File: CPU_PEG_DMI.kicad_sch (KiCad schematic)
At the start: 2 parts

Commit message: stroopwafel.exe
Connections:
- net DMI_CRx_PTx_0+: no longer JCPU1.Y3 (DMI_RXP_0)
- net DMI_CRx_PTx_0-: no longer JCPU1.Y4 (DMI_RXN_0)
- net DMI_CRx_PTx_1+: no longer JCPU1.AA4 (DMI_RXP_1)
- net DMI_CRx_PTx_1-: no longer JCPU1.AA5 (DMI_RXN_1)
- net DMI_CRx_PTx_2+: no longer JCPU1.AB4 (DMI_RXP_2)
- net DMI_CRx_PTx_2-: no longer JCPU1.AB3 (DMI_RXN_2)
- net DMI_CRx_PTx_3+: no longer JCPU1.AC4 (DMI_RXP_3)
- net DMI_CRx_PTx_3-: no longer JCPU1.AC5 (DMI_RXN_3)
- net DMI_CTx_PRx_0+: no longer JCPU1.AC2 (DMI_TXP_0)
- net DMI_CTx_PRx_0-: no longer JCPU1.AC1 (DMI_TXN_0)
- net DMI_CTx_PRx_1+: no longer JCPU1.AD3 (DMI_TXP_1)
- net DMI_CTx_PRx_1-: no longer JCPU1.AD2 (DMI_TXN_1)
- net DMI_CTx_PRx_2+: no longer JCPU1.AE2 (DMI_TXP_2)
- net DMI_CTx_PRx_2-: no longer JCPU1.AE1 (DMI_TXN_2)
- net DMI_CTx_PRx_3+: no longer JCPU1.AF2 (DMI_TXP_3)
- net DMI_CTx_PRx_3-: no longer JCPU1.AF3 (DMI_TXN_3)
- net PCIe_CPU_Rx0+: no longer JCPU1.B8 (PEG_RXP_0)
- net PCIe_CPU_Rx0-: no longer JCPU1.B7 (PEG_RXN_0)
- net PCIe_CPU_Rx1+: no longer JCPU1.C7 (PEG_RXP_1)
- net PCIe_CPU_Rx1-: no longer JCPU1.C6 (PEG_RXN_1)
- net PCIe_CPU_Rx10+: no longer JCPU1.M6 (PEG_RXP_10)
- net PCIe_CPU_Rx10-: no longer JCPU1.M5 (PEG_RXN_10)
- net PCIe_CPU_Rx11+: no longer JCPU1.N5 (PEG_RXP_11)
- net PCIe_CPU_Rx11-: no longer JCPU1.N4 (PEG_RXN_11)
- net PCIe_CPU_Rx12+: no longer JCPU1.P6 (PEG_RXP_12)
- net PCIe_CPU_Rx12-: no longer JCPU1.P5 (PEG_RXN_12)
- net PCIe_CPU_Rx13+: no longer JCPU1.R5 (PEG_RXP_13)
- net PCIe_CPU_Rx13-: no longer JCPU1.R4 (PEG_RXN_13)
- net PCIe_CPU_Rx14+: no longer JCPU1.T6 (PEG_RXP_14)
- net PCIe_CPU_Rx14-: no longer JCPU1.T5 (PEG_RXN_14)
- net PCIe_CPU_Rx15+: no longer JCPU1.U5 (PEG_RXP_15)
- net PCIe_CPU_Rx15-: no longer JCPU1.U4 (PEG_RXN_15)
- net PCIe_CPU_Rx2+: no longer JCPU1.D6 (PEG_RXP_2)
- net PCIe_CPU_Rx2-: no longer JCPU1.D5 (PEG_RXN_2)
- net PCIe_CPU_Rx3+: no longer JCPU1.E5 (PEG_RXP_3)
- net PCIe_CPU_Rx3-: no longer JCPU1.E4 (PEG_RXN_3)
- net PCIe_CPU_Rx4+: no longer JCPU1.F6 (PEG_RXP_4)
- net PCIe_CPU_Rx4-: no longer JCPU1.F5 (PEG_RXN_4)
- net PCIe_CPU_Rx5+: no longer JCPU1.G5 (PEG_RXP_5)
- net PCIe_CPU_Rx5-: no longer JCPU1.G4 (PEG_RXN_5)
- net PCIe_CPU_Rx6+: no longer JCPU1.H6 (PEG_RXP_6)
- net PCIe_CPU_Rx6-: no longer JCPU1.H5 (PEG_RXN_6)
- net PCIe_CPU_Rx7+: no longer JCPU1.J5 (PEG_RXP_7)
- net PCIe_CPU_Rx7-: no longer JCPU1.J4 (PEG_RXN_7)
- net PCIe_CPU_Rx8+: no longer JCPU1.K6 (PEG_RXP_8)
- net PCIe_CPU_Rx8-: no longer JCPU1.K5 (PEG_RXN_8)
- net PCIe_CPU_Rx9+: no longer JCPU1.L5 (PEG_RXP_9)
- net PCIe_CPU_Rx9-: no longer JCPU1.L4 (PEG_RXN_9)
- net PCIe_CPU_Tx0+: no longer JCPU1.A5 (PEG_TXP_0)
- net PCIe_CPU_Tx0-: no longer JCPU1.A6 (PEG_TXN_0)
- net PCIe_CPU_Tx1+: no longer JCPU1.B4 (PEG_TXP_1)
- net PCIe_CPU_Tx1-: no longer JCPU1.B5 (PEG_TXN_1)
- net PCIe_CPU_Tx10+: no longer JCPU1.L1 (PEG_TXP_10)
- net PCIe_CPU_Tx10-: no longer JCPU1.L2 (PEG_TXN_10)
- net PCIe_CPU_Tx11+: no longer JCPU1.M2 (PEG_TXP_11)
- net PCIe_CPU_Tx11-: no longer JCPU1.M3 (PEG_TXN_11)
- net PCIe_CPU_Tx12+: no longer JCPU1.N1 (PEG_TXP_12)
- net PCIe_CPU_Tx12-: no longer JCPU1.N2 (PEG_TXN_12)
- net PCIe_CPU_Tx13+: no longer JCPU1.P2 (PEG_TXP_13)
- net PCIe_CPU_Tx13-: no longer JCPU1.P3 (PEG_TXN_13)
- net PCIe_CPU_Tx14+: no longer JCPU1.R2 (PEG_TXP_14)
- net PCIe_CPU_Tx14-: no longer JCPU1.R1 (PEG_TXN_14)
- net PCIe_CPU_Tx15+: no longer JCPU1.T2 (PEG_TXP_15)
- net PCIe_CPU_Tx15-: no longer JCPU1.T3 (PEG_TXN_15)
- net PCIe_CPU_Tx2+: no longer JCPU1.C3 (PEG_TXP_2)
- net PCIe_CPU_Tx2-: no longer JCPU1.C4 (PEG_TXN_2)
- net PCIe_CPU_Tx3+: no longer JCPU1.D2 (PEG_TXP_3)
- net PCIe_CPU_Tx3-: no longer JCPU1.D3 (PEG_TXN_3)
- net PCIe_CPU_Tx4+: no longer JCPU1.E1 (PEG_TXP_4)
- net PCIe_CPU_Tx4-: no longer JCPU1.E2 (PEG_TXN_4)
- net PCIe_CPU_Tx5+: no longer JCPU1.F2 (PEG_TXP_5)
- net PCIe_CPU_Tx5-: no longer JCPU1.F3 (PEG_TXN_5)
- net PCIe_CPU_Tx6+: no longer JCPU1.G1 (PEG_TXP_6)
- net PCIe_CPU_Tx6-: no longer JCPU1.G2 (PEG_TXN_6)
- net PCIe_CPU_Tx7+: no longer JCPU1.H2 (PEG_TXP_7)
- net PCIe_CPU_Tx7-: no longer JCPU1.H3 (PEG_TXN_7)
- net PCIe_CPU_Tx8+: no longer JCPU1.J1 (PEG_TXP_8)
- net PCIe_CPU_Tx8-: no longer JCPU1.J2 (PEG_TXN_8)
- net PCIe_CPU_Tx9+: no longer JCPU1.K2 (PEG_TXP_9)
- net PCIe_CPU_Tx9-: no longer JCPU1.K3 (PEG_TXN_9)
- net at R10.2: no longer JCPU1.L7 (PEG_RCOMP)
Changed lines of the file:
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@@
 		(lib_id "A-my-stuff:Intel_CFL_1151")
 		(at 116.84 114.3 0)
-		(unit 3)
+		(unit 1)
 		(exclude_from_sim no)
 		(in_bom yes)
@@
 		(pin "J5"
 		)
-		(instances
-			(project ""
-				(path "/4bc771b8-eb19-46d0-8798-27231a7c6e83/061fe2d6-87c2-48c2-90bb-0928700512fc"
-					(reference "JCPU1")
-					(unit 3)
-				)
-			)
-		)
 	)

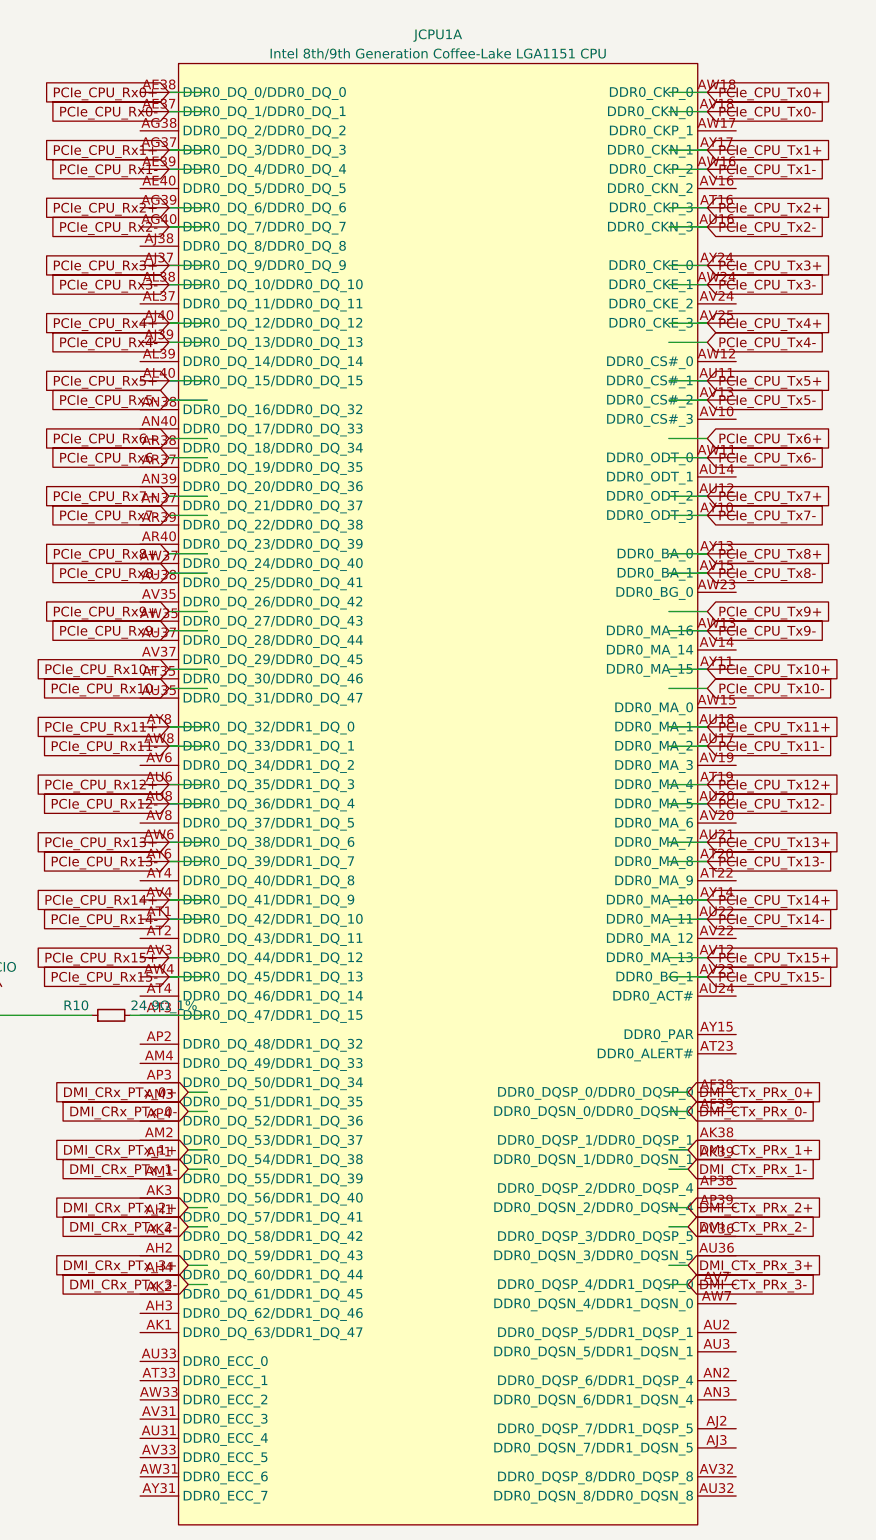
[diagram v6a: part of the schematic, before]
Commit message: Fixed entire schematic being broken
somehow every symbol with index 1 broke and updating the pcb stopped working. how does that even happen. oh well it's fixed now
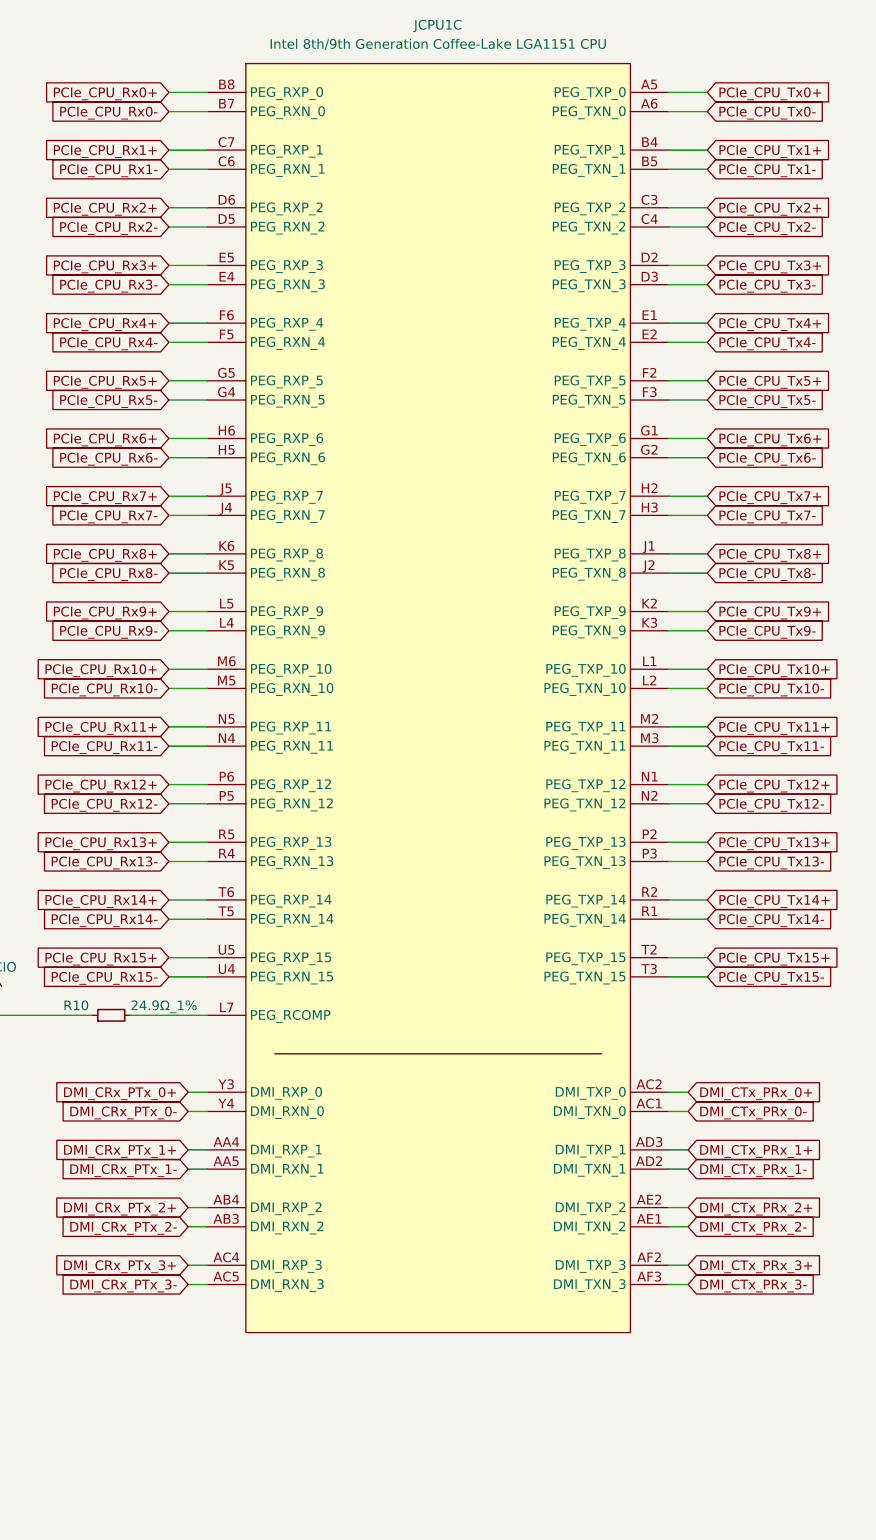
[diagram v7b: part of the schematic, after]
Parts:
- removed JCPU1: Intel 8th/9th Generation Coffee-Lake LGA1151 CPU, A-my-stuff:LGA-1151_L47.1-W42.5-P0.91_PE115127-4041-01H, symbol A-my-stuff:Intel_CFL_1151
- added JCPU1: Intel 8th/9th Generation Coffee-Lake LGA1151 CPU, A-my-stuff:LGA-1151_L47.1-W42.5-P0.91_PE115127-4041-01H, symbol A-my-stuff:Intel_CFL_1151
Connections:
- net DMI_CRx_PTx_0+: now also JCPU1.Y3 (DMI_RXP_0)
- net DMI_CRx_PTx_0-: now also JCPU1.Y4 (DMI_RXN_0)
- net DMI_CRx_PTx_1+: now also JCPU1.AA4 (DMI_RXP_1)
- net DMI_CRx_PTx_1-: now also JCPU1.AA5 (DMI_RXN_1)
- net DMI_CRx_PTx_2+: now also JCPU1.AB4 (DMI_RXP_2)
- net DMI_CRx_PTx_2-: now also JCPU1.AB3 (DMI_RXN_2)
- net DMI_CRx_PTx_3+: now also JCPU1.AC4 (DMI_RXP_3)
- net DMI_CRx_PTx_3-: now also JCPU1.AC5 (DMI_RXN_3)
- net DMI_CTx_PRx_0+: now also JCPU1.AC2 (DMI_TXP_0)
- net DMI_CTx_PRx_0-: now also JCPU1.AC1 (DMI_TXN_0)
- net DMI_CTx_PRx_1+: now also JCPU1.AD3 (DMI_TXP_1)
- net DMI_CTx_PRx_1-: now also JCPU1.AD2 (DMI_TXN_1)
- net DMI_CTx_PRx_2+: now also JCPU1.AE2 (DMI_TXP_2)
- net DMI_CTx_PRx_2-: now also JCPU1.AE1 (DMI_TXN_2)
- net DMI_CTx_PRx_3+: now also JCPU1.AF2 (DMI_TXP_3)
- net DMI_CTx_PRx_3-: now also JCPU1.AF3 (DMI_TXN_3)
- net PCIe_CPU_Rx0+: now also JCPU1.B8 (PEG_RXP_0)
- net PCIe_CPU_Rx0-: now also JCPU1.B7 (PEG_RXN_0)
- net PCIe_CPU_Rx1+: now also JCPU1.C7 (PEG_RXP_1)
- net PCIe_CPU_Rx1-: now also JCPU1.C6 (PEG_RXN_1)
- net PCIe_CPU_Rx10+: now also JCPU1.M6 (PEG_RXP_10)
- net PCIe_CPU_Rx10-: now also JCPU1.M5 (PEG_RXN_10)
- net PCIe_CPU_Rx11+: now also JCPU1.N5 (PEG_RXP_11)
- net PCIe_CPU_Rx11-: now also JCPU1.N4 (PEG_RXN_11)
- net PCIe_CPU_Rx12+: now also JCPU1.P6 (PEG_RXP_12)
- net PCIe_CPU_Rx12-: now also JCPU1.P5 (PEG_RXN_12)
- net PCIe_CPU_Rx13+: now also JCPU1.R5 (PEG_RXP_13)
- net PCIe_CPU_Rx13-: now also JCPU1.R4 (PEG_RXN_13)
- net PCIe_CPU_Rx14+: now also JCPU1.T6 (PEG_RXP_14)
- net PCIe_CPU_Rx14-: now also JCPU1.T5 (PEG_RXN_14)
- net PCIe_CPU_Rx15+: now also JCPU1.U5 (PEG_RXP_15)
- net PCIe_CPU_Rx15-: now also JCPU1.U4 (PEG_RXN_15)
- net PCIe_CPU_Rx2+: now also JCPU1.D6 (PEG_RXP_2)
- net PCIe_CPU_Rx2-: now also JCPU1.D5 (PEG_RXN_2)
- net PCIe_CPU_Rx3+: now also JCPU1.E5 (PEG_RXP_3)
- net PCIe_CPU_Rx3-: now also JCPU1.E4 (PEG_RXN_3)
- net PCIe_CPU_Rx4+: now also JCPU1.F6 (PEG_RXP_4)
- net PCIe_CPU_Rx4-: now also JCPU1.F5 (PEG_RXN_4)
- net PCIe_CPU_Rx5+: now also JCPU1.G5 (PEG_RXP_5)
- net PCIe_CPU_Rx5-: now also JCPU1.G4 (PEG_RXN_5)
- net PCIe_CPU_Rx6+: now also JCPU1.H6 (PEG_RXP_6)
- net PCIe_CPU_Rx6-: now also JCPU1.H5 (PEG_RXN_6)
- net PCIe_CPU_Rx7+: now also JCPU1.J5 (PEG_RXP_7)
- net PCIe_CPU_Rx7-: now also JCPU1.J4 (PEG_RXN_7)
- net PCIe_CPU_Rx8+: now also JCPU1.K6 (PEG_RXP_8)
- net PCIe_CPU_Rx8-: now also JCPU1.K5 (PEG_RXN_8)
- net PCIe_CPU_Rx9+: now also JCPU1.L5 (PEG_RXP_9)
- net PCIe_CPU_Rx9-: now also JCPU1.L4 (PEG_RXN_9)
- net PCIe_CPU_Tx0+: now also JCPU1.A5 (PEG_TXP_0)
- net PCIe_CPU_Tx0-: now also JCPU1.A6 (PEG_TXN_0)
- net PCIe_CPU_Tx1+: now also JCPU1.B4 (PEG_TXP_1)
- net PCIe_CPU_Tx1-: now also JCPU1.B5 (PEG_TXN_1)
- net PCIe_CPU_Tx10+: now also JCPU1.L1 (PEG_TXP_10)
- net PCIe_CPU_Tx10-: now also JCPU1.L2 (PEG_TXN_10)
- net PCIe_CPU_Tx11+: now also JCPU1.M2 (PEG_TXP_11)
- net PCIe_CPU_Tx11-: now also JCPU1.M3 (PEG_TXN_11)
- net PCIe_CPU_Tx12+: now also JCPU1.N1 (PEG_TXP_12)
- net PCIe_CPU_Tx12-: now also JCPU1.N2 (PEG_TXN_12)
- net PCIe_CPU_Tx13+: now also JCPU1.P2 (PEG_TXP_13)
- net PCIe_CPU_Tx13-: now also JCPU1.P3 (PEG_TXN_13)
- net PCIe_CPU_Tx14+: now also JCPU1.R2 (PEG_TXP_14)
- net PCIe_CPU_Tx14-: now also JCPU1.R1 (PEG_TXN_14)
- net PCIe_CPU_Tx15+: now also JCPU1.T2 (PEG_TXP_15)
- net PCIe_CPU_Tx15-: now also JCPU1.T3 (PEG_TXN_15)
- net PCIe_CPU_Tx2+: now also JCPU1.C3 (PEG_TXP_2)
- net PCIe_CPU_Tx2-: now also JCPU1.C4 (PEG_TXN_2)
- net PCIe_CPU_Tx3+: now also JCPU1.D2 (PEG_TXP_3)
- net PCIe_CPU_Tx3-: now also JCPU1.D3 (PEG_TXN_3)
- net PCIe_CPU_Tx4+: now also JCPU1.E1 (PEG_TXP_4)
- net PCIe_CPU_Tx4-: now also JCPU1.E2 (PEG_TXN_4)
- net PCIe_CPU_Tx5+: now also JCPU1.F2 (PEG_TXP_5)
- net PCIe_CPU_Tx5-: now also JCPU1.F3 (PEG_TXN_5)
- net PCIe_CPU_Tx6+: now also JCPU1.G1 (PEG_TXP_6)
- net PCIe_CPU_Tx6-: now also JCPU1.G2 (PEG_TXN_6)
- net PCIe_CPU_Tx7+: now also JCPU1.H2 (PEG_TXP_7)
- net PCIe_CPU_Tx7-: now also JCPU1.H3 (PEG_TXN_7)
- net PCIe_CPU_Tx8+: now also JCPU1.J1 (PEG_TXP_8)
- net PCIe_CPU_Tx8-: now also JCPU1.J2 (PEG_TXN_8)
- net PCIe_CPU_Tx9+: now also JCPU1.K2 (PEG_TXP_9)
- net PCIe_CPU_Tx9-: now also JCPU1.K3 (PEG_TXN_9)
- net at R10.2: now also JCPU1.L7 (PEG_RCOMP)

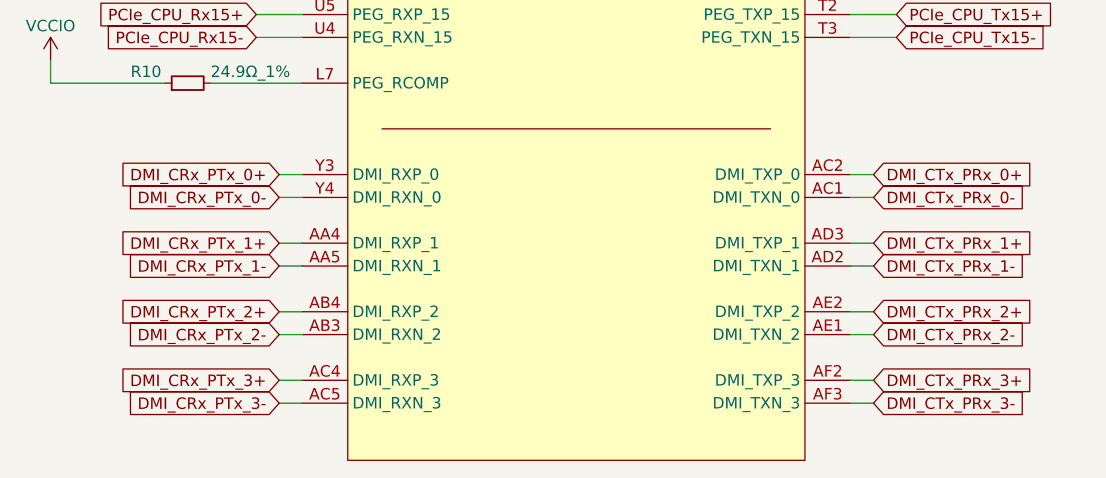
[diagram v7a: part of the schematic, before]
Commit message: Added interconnect between CPU and PCH boards and added ATX board outline
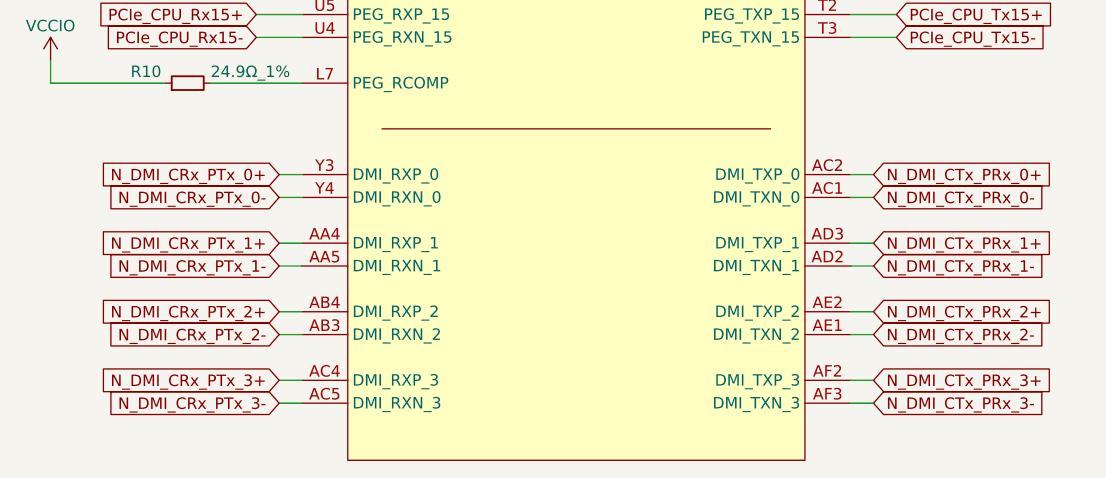
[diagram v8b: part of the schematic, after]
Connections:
- net DMI_CRx_PTx_0+ renamed N_DMI_CRx_PTx_0+
- net DMI_CRx_PTx_0- renamed N_DMI_CRx_PTx_0-
- net DMI_CRx_PTx_1+ renamed N_DMI_CRx_PTx_1+
- net DMI_CRx_PTx_1- renamed N_DMI_CRx_PTx_1-
- net DMI_CRx_PTx_2+ renamed N_DMI_CRx_PTx_2+
- net DMI_CRx_PTx_2- renamed N_DMI_CRx_PTx_2-
- net DMI_CRx_PTx_3+ renamed N_DMI_CRx_PTx_3+
- net DMI_CRx_PTx_3- renamed N_DMI_CRx_PTx_3-
- net DMI_CTx_PRx_0+ renamed N_DMI_CTx_PRx_0+
- net DMI_CTx_PRx_0- renamed N_DMI_CTx_PRx_0-
- net DMI_CTx_PRx_1+ renamed N_DMI_CTx_PRx_1+
- net DMI_CTx_PRx_1- renamed N_DMI_CTx_PRx_1-
- net DMI_CTx_PRx_2+ renamed N_DMI_CTx_PRx_2+
- net DMI_CTx_PRx_2- renamed N_DMI_CTx_PRx_2-
- net DMI_CTx_PRx_3+ renamed N_DMI_CTx_PRx_3+
- net DMI_CTx_PRx_3- renamed N_DMI_CTx_PRx_3-
